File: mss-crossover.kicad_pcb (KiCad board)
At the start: 2 copper layers, 50.8 x 61.8 mm, 20 parts, among them J1 2x-screw, J2 RJ45, J4 2x-screw, J7 RJ45, Q1 2N3904

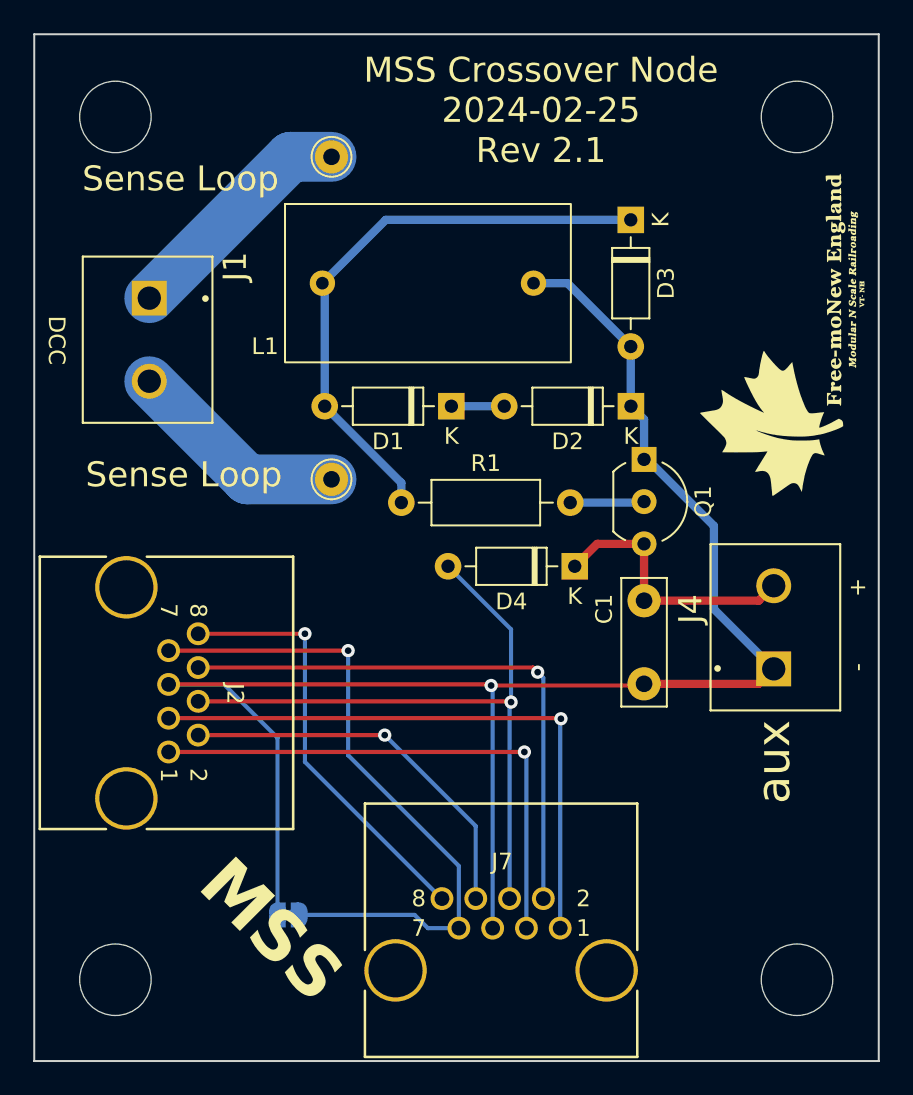
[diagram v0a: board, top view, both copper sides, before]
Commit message: Changed connectors to MJ3221-88 (the yellow ones that Ryan found) and put the connectors on opposite edges of the board (like everyone but me likes).  Also updated the footprint for the pulse transformer to have larger holes and to include the unused center pin.
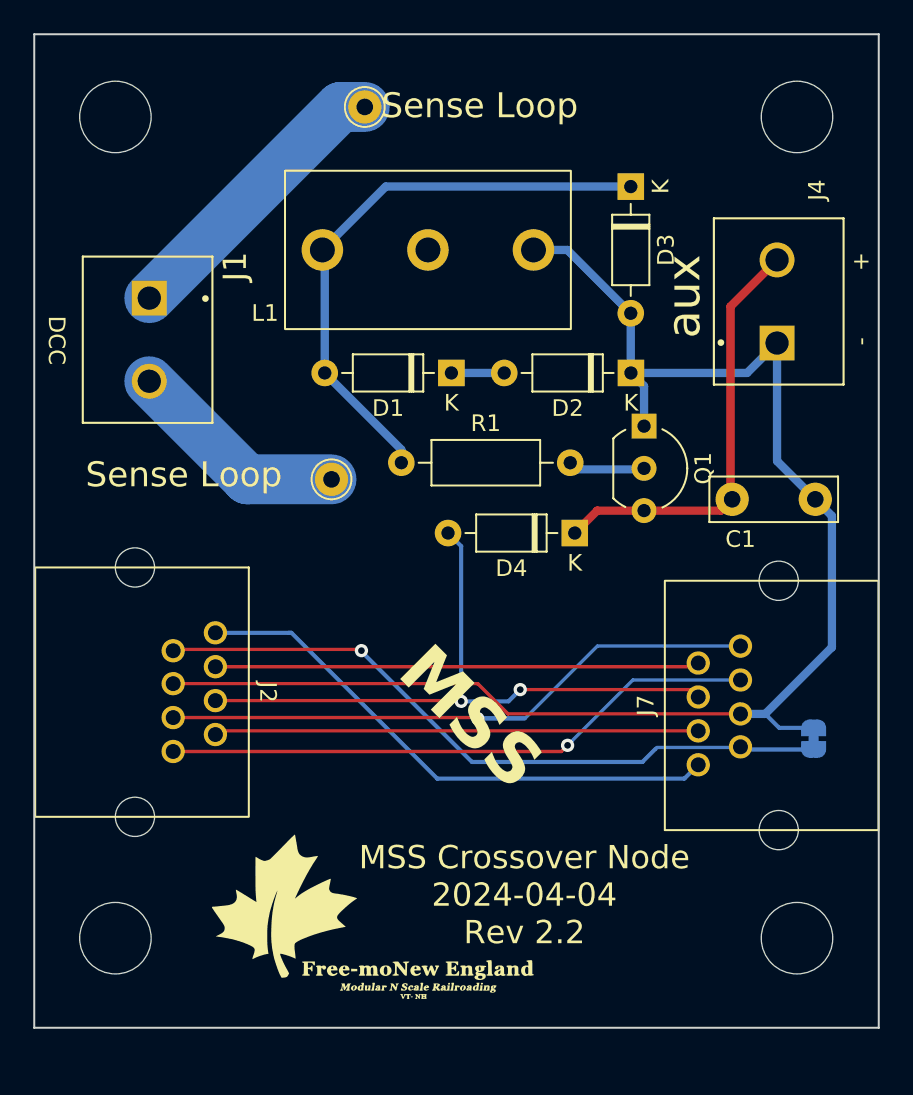
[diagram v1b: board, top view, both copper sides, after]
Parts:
- J2, J7: footprint Imports:CONN_RJSBE5080_16P13X12P57_AMP -> myMods:MJ3221-88
- L1: footprint myMods:FIS101NL -> myMods:Murata_56300C
- moved G*** 43.2 mm to (126.2, 109.0), turned to 0 degrees
- moved JP1 33.3 mm to (152.8, 98.0), turned to 90 degrees
- moved J4 19.6 mm to (150.6, 74.2)
- moved J7 17.2 mm to (148.4, 96.0), turned to 90 degrees
- moved C1 8.08 mm to (147.9, 83.6), turned to 0 degrees
- moved J2 3.61 mm to (114.3, 95.2)
- moved TP1 3.61 mm to (125.8, 60.0)
- moved REF** 2.50 mm to (110.8, 110.0)
- moved REF** 2.50 mm to (151.8, 110.0)
- moved R1 2.40 mm to (128.0, 81.4)
- moved D1 2.00 mm to (131.0, 76.0)
- moved D2 2.00 mm to (141.8, 76.0)
- moved D3 2.00 mm to (141.8, 64.8)
- moved D4 2.00 mm to (138.4, 85.6)
- moved L1 2.00 mm to (129.6, 68.6)
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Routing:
- net /MSS GND: track 100.5 -> 89.0 mm, vias 1 -> 0
- net Net-(D4-K): track 16.3 -> 25.8 mm
- net /AD A: track 25.8 -> 33.0 mm, vias 1 -> 0
- net /Ain A: track 23.3 -> 29.1 mm, vias 1 -> 0
- net /Ain B: track 34.3 -> 29.1 mm, vias 1 -> 0
- net /AAin A: track 32.0 -> 35.9 mm
- net Net-(J1-Pin_1): track 14.5 -> 17.7 mm
- net /AAin B: track 36.2 -> 38.8 mm
- net /7 A: track 40.2 -> 41.8 mm
- net /Local A: track 40.4 -> 40.1 mm, vias 1 -> 2
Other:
- board size 50.8 x 61.8 mm -> 50.8 x 59.8 mm
